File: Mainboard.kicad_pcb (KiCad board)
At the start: 4 copper layers, 90.2 x 95.9 mm, 244 parts, among them J1 USB_C_Receptacle_USB2.0, J10 200528-0100, J11 200528-0100, J12 200528-0100, J13 200528-0100, J14 200528-0100, J15 200528-0100, J16 200528-0100, J17 200528-0100, J18 200528-0100, J19 Conn_01x09, J2 282834-4, J20 Conn_01x04, J21 Conn_01x06, J22 U.FL-R-SMT-1, J23 U.FL-R-SMT-1, J24 Conn_02x05_Odd_Even, J3 282834-4, J4 1985807, J5 1985807, J6 1985807, J7 USB_C_Receptacle_USB2.0, J8 Micro_SD_Card_Det2, J9 Conn_02x05_Odd_Even, Q1 IRLML2803, Q10 MBT2222ADW1T1, Q11 BSS138DWQ-7, Q12 MBT2222ADW1T1, Q13 BSS138DWQ-7, Q14 MBT2222ADW1T1, Q15 BSS138DWQ-7, Q16 MMBT2907, Q17 MMBT2907, Q18 IRLML2803, Q19 IRF7404, Q2 MBT2222ADW1T1, Q21 IRLML2803, Q22 IRLML2803, Q23 IRF7404, Q3 MBT2222ADW1T1, Q4 MBT2222ADW1T1, Q5 BSS138DWQ-7, Q6 MBT2222ADW1T1, Q7 BSS138DWQ-7, Q8 MBT2222ADW1T1, Q9 BSS138DWQ-7, SW1 KMR231NG LFS, SW2 KMR231NG LFS, U1 MAX706RESA+, U10 ATSAMD21E18A-A, U11 MAX706RESA+, U12 E22-900M30S, U13 S1216V8, U14 EP2W+, U15 USBLC6-2SC6, U16 USBLC6-2SC6, U2 ATSAMD51J20A-AU, U3 BMX160, U4 DS3231S, U5 MR25H40MDF, U6 TPS7A4501DCQT, U7 TPS54226PWPR, U8 BQ25883RGER, U9 ADM1176-1ARMZ-R7, Y1 32.768kHz, Y2 32.768kHz

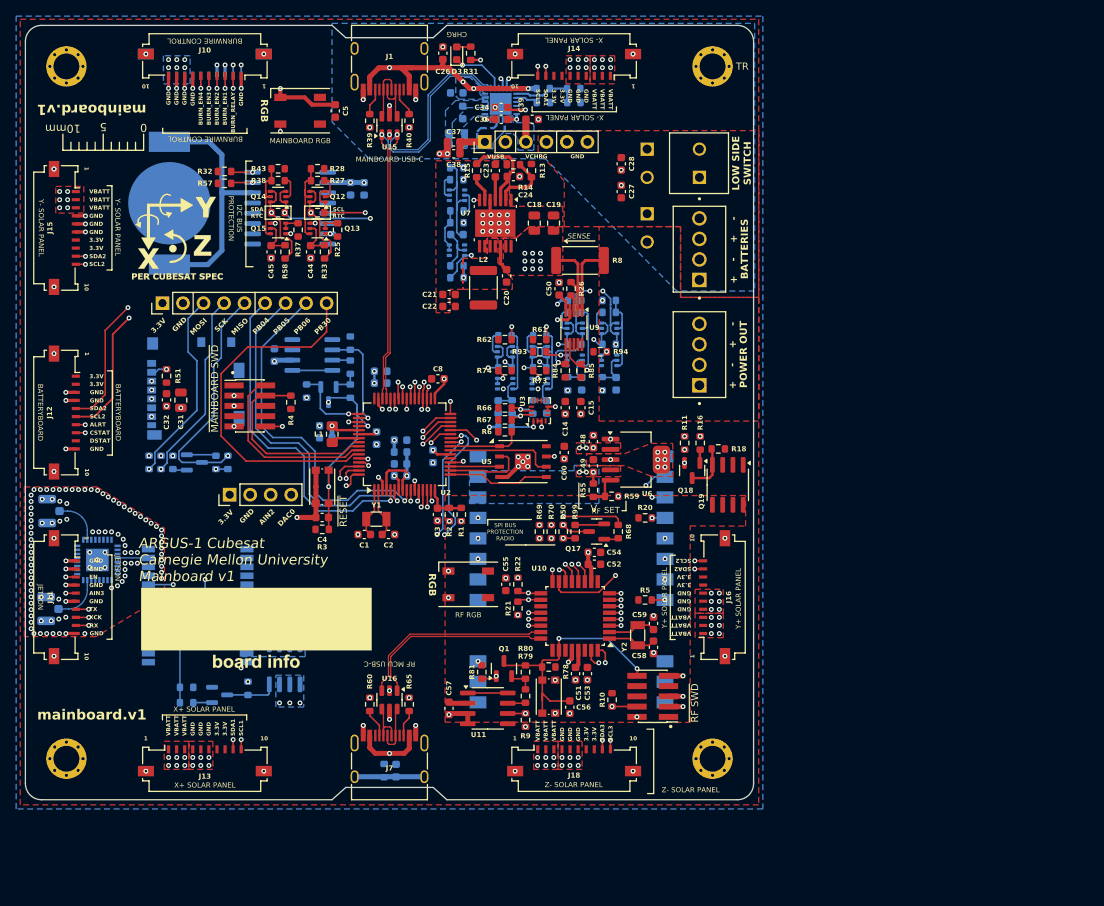
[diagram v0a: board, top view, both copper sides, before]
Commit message: Updated Mounting Holes
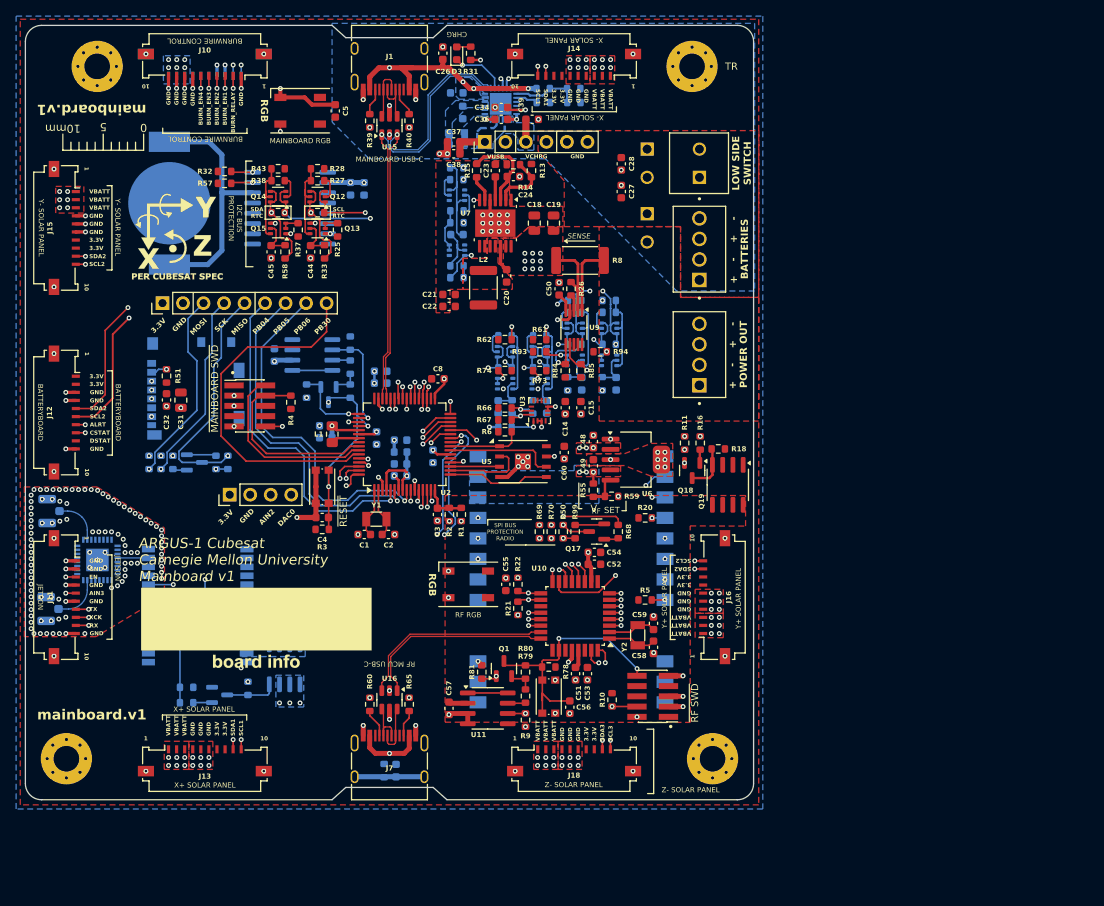
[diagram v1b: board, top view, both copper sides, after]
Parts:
- H1, H2, H3, H4: footprint mainboard:MountingHole -> mainboard:MountingHole2
- moved H1 3.81 mm to (108.6, 58.4)
- moved H2 2.54 mm to (182.2, 58.4)
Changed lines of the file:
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@@
 		)
 	)
-	(footprint "mainboard:MountingHole"
+	(footprint "mainboard:MountingHole2"
 		(layer "F.Cu")
-		(at 104.775 58.42)
+		(at 108.585 58.42)
 		(descr "Mounting Hole 3.2mm, M3")
 		(tags "mounting hole 3.2mm m3")
@@
 			)
 		)
-		(property "Footprint" "mainboard:MountingHole"
+		(property "Footprint" "mainboard:MountingHole2"
 			(at 0 0 0)
 			(layer "F.Fab")
@@
 		)
 		(pad "1" thru_hole circle
-			(at -2.05 0)
+			(at -2.38125 0 180)
 			(size 0.762 0.762)
 			(drill 0.381)
@@
 		)
 		(pad "1" thru_hole circle
-			(at -1.4495 -1.4495)
+			(at -1.683798 -1.683798 315)
 			(size 0.762 0.762)
 			(drill 0.381)
@@
 		)
 		(pad "1" thru_hole circle
-			(at -1.4495 1.4495)
+			(at -1.683798 1.683798 315)
 			(size 0.762 0.762)
 			(drill 0.381)
@@
 		)
 		(pad "1" thru_hole circle
-			(at 0 -2.05)
+			(at 0 -2.38125 180)
 			(size 0.762 0.762)
 			(drill 0.381)
@@
 		(pad "1" thru_hole circle
 			(at 0 0)
-			(size 5 5)
-			(drill 3.2)
+			(size 6.35 6.35)
+			(drill 3.175)
 			(layers "*.Cu" "*.Mask")
 			(remove_unused_layers no)
@@
 		)
 		(pad "1" thru_hole circle
-			(at 0 2.05)
+			(at 0 2.38125 180)
 			(size 0.762 0.762)
 			(drill 0.381)
@@
 		)
 		(pad "1" thru_hole circle
-			(at 1.4495 -1.4495)
+			(at 1.683798 -1.683798 315)
 			(size 0.762 0.762)
 			(drill 0.381)
@@
 		)
 		(pad "1" thru_hole circle
-			(at 1.4495 1.4495)
+			(at 1.683798 1.683798 315)
 			(size 0.762 0.762)
 			(drill 0.381)
@@
 		)
 		(pad "1" thru_hole circle
-			(at 2.05 0)
+			(at 2.38125 0 180)
 			(size 0.762 0.762)
 			(drill 0.381)
@@
 		)
 	)
-	(footprint "mainboard:MountingHole"
+	(footprint "mainboard:MountingHole2"
 		(layer "F.Cu")
 		(at 184.785 144.145)
@@
 			)
 		)
-		(property "Footprint" "mainboard:MountingHole"
+		(property "Footprint" "mainboard:MountingHole2"
 			(at 0 0 0)
 			(layer "F.Fab")
@@
 		)
 		(pad "1" thru_hole circle
-			(at -2.05 0)
+			(at -2.38125 0 180)
 			(size 0.762 0.762)
 			(drill 0.381)
@@
 		)
 		(pad "1" thru_hole circle
-			(at -1.4495 -1.4495)
+			(at -1.683798 -1.683798 315)
 			(size 0.762 0.762)
 			(drill 0.381)
@@
 		)
 		(pad "1" thru_hole circle
-			(at -1.4495 1.4495)
+			(at -1.683798 1.683798 315)
 			(size 0.762 0.762)
 			(drill 0.381)
@@
 		)
 		(pad "1" thru_hole circle
-			(at 0 -2.05)
+			(at 0 -2.38125 180)
 			(size 0.762 0.762)
 			(drill 0.381)
@@
 		(pad "1" thru_hole circle
 			(at 0 0)
-			(size 5 5)
-			(drill 3.2)
+			(size 6.35 6.35)
+			(drill 3.175)
 			(layers "*.Cu" "*.Mask")
 			(remove_unused_layers no)
@@
 		)
 		(pad "1" thru_hole circle
-			(at 0 2.05)
+			(at 0 2.38125 180)
 			(size 0.762 0.762)
 			(drill 0.381)
@@
 		)
 		(pad "1" thru_hole circle
-			(at 1.4495 -1.4495)
+			(at 1.683798 -1.683798 315)
 			(size 0.762 0.762)
 			(drill 0.381)
@@
 		)
 		(pad "1" thru_hole circle
-			(at 1.4495 1.4495)
+			(at 1.683798 1.683798 315)
 			(size 0.762 0.762)
 			(drill 0.381)
@@
 		)
 		(pad "1" thru_hole circle
-			(at 2.05 0)
+			(at 2.38125 0 180)
 			(size 0.762 0.762)
 			(drill 0.381)
@@
 			(layers "F.Cu" "F.Paste" "F.Mask")
 			(net 4 "~{RESET}")
-			(pinfunction "P")
+			(pinfunction "P1")
 			(pintype "passive")
 		)
@@
 			(layers "F.Cu" "F.Paste" "F.Mask")
 			(net 4 "~{RESET}")
-			(pinfunction "P")
+			(pinfunction "P1")
 			(pintype "passive")
 		)
@@
 			(layers "F.Cu" "F.Paste" "F.Mask")
 			(net 6 "GND")
-			(pinfunction "S1")
+			(pinfunction "S")
 			(pintype "passive")
 		)
@@
 			(layers "F.Cu" "F.Paste" "F.Mask")
 			(net 6 "GND")
-			(pinfunction "S1")
+			(pinfunction "S")
 			(pintype "passive")
 		)
@@
 		)
 	)
-	(footprint "mainboard:MountingHole"
+	(footprint "mainboard:MountingHole2"
 		(layer "F.Cu")
-		(at 184.785 58.42)
+		(at 182.245 58.42)
 		(descr "Mounting Hole 3.2mm, M3")
 		(tags "mounting hole 3.2mm m3")
@@
 			)
 		)
-		(property "Footprint" "mainboard:MountingHole"
+		(property "Footprint" "mainboard:MountingHole2"
 			(at 0 0 0)
 			(layer "F.Fab")
@@
 		)
 		(pad "1" thru_hole circle
-			(at -2.05 0)
+			(at -2.38125 0 180)
 			(size 0.762 0.762)
 			(drill 0.381)
@@
 		)
 		(pad "1" thru_hole circle
-			(at -1.4495 -1.4495)
+			(at -1.683798 -1.683798 315)
 			(size 0.762 0.762)
 			(drill 0.381)
@@
 		)
 		(pad "1" thru_hole circle
-			(at -1.4495 1.4495)
+			(at -1.683798 1.683798 315)
 			(size 0.762 0.762)
 			(drill 0.381)
@@
 		)
 		(pad "1" thru_hole circle
-			(at 0 -2.05)
+			(at 0 -2.38125 180)
 			(size 0.762 0.762)
 			(drill 0.381)
@@
 		(pad "1" thru_hole circle
 			(at 0 0)
-			(size 5 5)
-			(drill 3.2)
+			(size 6.35 6.35)
+			(drill 3.175)
 			(layers "*.Cu" "*.Mask")
 			(remove_unused_layers no)
@@
 		)
 		(pad "1" thru_hole circle
-			(at 0 2.05)
+			(at 0 2.38125 180)
 			(size 0.762 0.762)
 			(drill 0.381)
@@
 		)
 		(pad "1" thru_hole circle
-			(at 1.4495 -1.4495)
+			(at 1.683798 -1.683798 315)
 			(size 0.762 0.762)
 			(drill 0.381)
@@
 		)
 		(pad "1" thru_hole circle
-			(at 1.4495 1.4495)
+			(at 1.683798 1.683798 315)
 			(size 0.762 0.762)
 			(drill 0.381)
@@
 		)
 		(pad "1" thru_hole circle
-			(at 2.05 0)
+			(at 2.38125 0 180)
 			(size 0.762 0.762)
 			(drill 0.381)
@@
 		)
 	)
-	(footprint "mainboard:MountingHole"
+	(footprint "mainboard:MountingHole2"
 		(layer "F.Cu")
 		(at 104.775 144.145)
@@
 			)
 		)
-		(property "Footprint" "mainboard:MountingHole"
+		(property "Footprint" "mainboard:MountingHole2"
 			(at 0 0 0)
 			(layer "F.Fab")
@@
 		)
 		(pad "1" thru_hole circle
-			(at -2.05 0)
+			(at -2.38125 0 180)
 			(size 0.762 0.762)
 			(drill 0.381)
@@
 		)
 		(pad "1" thru_hole circle
-			(at -1.4495 -1.4495)
+			(at -1.683798 -1.683798 315)
 			(size 0.762 0.762)
 			(drill 0.381)
@@
 		)
 		(pad "1" thru_hole circle
-			(at -1.4495 1.4495)
+			(at -1.683798 1.683798 315)
 			(size 0.762 0.762)
 			(drill 0.381)
@@
 		)
 		(pad "1" thru_hole circle
-			(at 0 -2.05)
+			(at 0 -2.38125 180)
 			(size 0.762 0.762)
 			(drill 0.381)
@@
 		(pad "1" thru_hole circle
 			(at 0 0)
-			(size 5 5)
-			(drill 3.2)
+			(size 6.35 6.35)
+			(drill 3.175)
 			(layers "*.Cu" "*.Mask")
 			(remove_unused_layers no)
@@
 		)
 		(pad "1" thru_hole circle
-			(at 0 2.05)
+			(at 0 2.38125 180)
 			(size 0.762 0.762)
 			(drill 0.381)
@@
 		)
 		(pad "1" thru_hole circle
-			(at 1.4495 -1.4495)
+			(at 1.683798 -1.683798 315)
 			(size 0.762 0.762)
 			(drill 0.381)
@@
 		)
 		(pad "1" thru_hole circle
-			(at 1.4495 1.4495)
+			(at 1.683798 1.683798 315)
 			(size 0.762 0.762)
 			(drill 0.381)
@@
 		)
 		(pad "1" thru_hole circle
-			(at 2.05 0)
+			(at 2.38125 0 180)
 			(size 0.762 0.762)
 			(drill 0.381)
@@
 	)
 	(gr_text "TR"
-		(at 188.468 58.42 0)
+		(at 187.1218 58.42 0)
 		(layer "F.SilkS")
 		(effects

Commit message: v1 Final
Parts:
- R59: value 2.5K -> 3.16K
- REF** (x2): moved to B.Cu
- moved REF** 56.6 mm to (117.9, 78.6), turned to 180 degrees
- moved REF** 56.0 mm to (107.8, 134.8), turned to 180 degrees
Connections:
- net JETSON_RX renamed JETSON_MISO
- net JETSON_TX renamed JETSON_MOSI
- net JETSON_XCK renamed JETSON_SCK
- J11 pad 1: GND -> 3.3V
- J11 pad 2: GND -> SDA1
- J11 pad 3: JETSON_EN -> SCL1
- J11 pad 4: GND -> JETSON_EN
- J11 pad 5: AIN3 -> GND
- J11 pad 6: GND -> JETSON_CS
- J19 pad 8: PB06 -> GND
- U2 pad 10: JETSON_EN -> JETSON_CS
- U2 pad 9: PB06 -> JETSON_EN
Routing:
- net AIN3: track 62.6 -> 0.00 mm, vias 2 -> 0
- net JETSON_CS: track 0.00 -> 61.9 mm, vias 0 -> 2
- net PB06: track 44.5 -> 0.00 mm, vias 1 -> 0
- net SCL1: track 145.8 -> 185.9 mm, vias 6 -> 9
- net SDA1: track 136.8 -> 176.1 mm, vias 6 -> 9
- net 3.3V: track 14.8 -> 31.3 mm, vias 18 -> 20
- net GND: track 79.0 -> 75.3 mm, vias 246 -> 240
- net JETSON_EN: track 61.9 -> 61.3 mm
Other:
- board text removed: "AIN3"
- board text removed: "RX"
- board text removed: "TX"
- board text removed: "XCK"

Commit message: v1.1 Schematic
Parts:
- added C61: 0.1uF, Capacitor_SMD:C_0603_1608Metric, F.Cu at (168.4, 120.4)
- added C62: 0.1uF, Capacitor_SMD:C_0603_1608Metric, F.Cu at (164.8, 133.1)
- added C63: 0.1uF, Capacitor_SMD:C_0603_1608Metric, F.Cu at (204.9, 129.1)
- added C64: 0.1uF, Capacitor_SMD:C_0603_1608Metric, F.Cu at (166.1, 120.4)
- added C65: 0.1uF, Capacitor_SMD:C_0603_1608Metric, F.Cu at (168.4, 133.1)
- added C66: 0.1uF, Capacitor_SMD:C_0603_1608Metric, F.Cu at (173.8, 126.3)
- added C67: 10uF, Capacitor_SMD:C_0603_1608Metric, F.Cu at (160.2, 120.4)
- added C68: 10uF, Capacitor_SMD:C_0603_1608Metric, F.Cu at (163.1, 120.4)
- added C69: 0.1uF, Capacitor_SMD:C_0603_1608Metric, F.Cu at (164.6, 120.4)
- added C70: 0.1uF, Capacitor_SMD:C_0603_1608Metric, F.Cu at (161.0, 126.7)
- added C71: 1uF, Capacitor_SMD:C_0603_1608Metric, F.Cu at (208.9, 124.1)
- added D4: GREEN LED, LED_SMD:LED_0603_1608Metric, F.Cu at (222.6, 128.1)
- added FB2: FerriteBead_Small, Inductor_SMD:L_0603_1608Metric, F.Cu at (161.7, 120.4)
- added R100: 27R, Resistor_SMD:R_0603_1608Metric, F.Cu at (157.1, 126.4)
- added R101: 27R, Resistor_SMD:R_0603_1608Metric, F.Cu at (157.1, 124.9)
- added R102: 0R, Resistor_SMD:R_0603_1608Metric, F.Cu at (212.9, 121.6)
- added R103: 0R, Resistor_SMD:R_0603_1608Metric, F.Cu at (212.9, 124.1)
- added R104: 10K, Resistor_SMD:R_0603_1608Metric, F.Cu at (212.9, 126.6)
- added R105: 1K, Resistor_SMD:R_0603_1608Metric, F.Cu at (227.5, 130.4)
- added SW3: KMR231NG LFS, Button_Switch_SMD:SW_Push_1P1T_NO_CK_KMR2, F.Cu at (228.8, 126.9)
- added U17: RP2040, Package_DFN_QFN:QFN-56-1EP_7x7mm_P0.4mm_EP3.2x3.2mm, F.Cu at (167.4, 126.9)
- C54: value 10uF -> 0.1uF
- C58, C59: value 8pF -> 15pF
- R10: value 10K -> 1K
- U10: value ATSAMD21E18A-A -> MR25H40MDF; footprint Package_QFP:TQFP-32_7x7mm_P0.8mm -> Package_DFN_QFN:DFN-8-1EP_6x5mm_P1.27mm_EP2x2mm
- Y2: value 32.768kHz -> ABM8-272-T3; footprint Crystal:Crystal_SMD_3215-2Pin_3.2x1.5mm -> Crystal:Crystal_SMD_3225-4Pin_3.2x2.5mm
- moved D2 66.0 mm to (212.5, 91.0), turned to -90 degrees
- moved C55 64.3 mm to (212.5, 86.6), turned to 180 degrees
- moved C57 60.6 mm to (205.8, 109.8), turned to 0 degrees
- moved R9 60.1 mm to (207.3, 100.3), turned to 0 degrees
- moved U11 58.9 mm to (205.8, 105.0), turned to 90 degrees
- moved R79 55.9 mm to (204.3, 100.3), turned to 0 degrees
- moved J24 54.3 mm to (222.1, 105.6)
- moved R81 52.9 mm to (201.3, 105.7), turned to 180 degrees
- moved R80 51.7 mm to (201.3, 100.3), turned to 0 degrees
- moved Q1 51.6 mm to (200.9, 103.0), turned to 180 degrees
- moved R22 49.6 mm to (208.9, 134.1), turned to 0 degrees
- moved R21 48.6 mm to (208.9, 131.6), turned to 0 degrees
- moved C56 44.3 mm to (205.9, 116.3), turned to -90 degrees
- moved SW2 42.8 mm to (202.3, 116.3), turned to 180 degrees
- moved R78 37.9 mm to (198.6, 116.3), turned to -90 degrees
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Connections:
- C51 pad 1: Net-(U10-VDDCORE) -> +1V2
- C52 pad 1: RF_3.3V -> +1V2
- C53 pad 1: RF_3.3V -> +1V2
- C56 pad 2: ~{SAMD21_RST} -> ~{RF_RST}
- C58 pad 1: Net-(U10-PA00) -> Net-(U17-XIN)
- C59 pad 1: Net-(U10-PA01) -> Net-(C59-Pad1)
- D2 pad 4: /RF and GPS/SAMD21_NEOPIXEL -> /RF and GPS/RF_NEOPIXEL
- J24 pad 10: ~{SAMD21_RST} -> ~{RF_RST}
- J24 pad 2: SAMD21_SWD -> RF_SWD
- J24 pad 4: SAMD21_SWC -> RF_SWC
- Q1 pad 1: SAMD21_WDT_EN -> RF_WDT_EN
- Q1 pad 3: ~{SAMD21_RST} -> ~{RF_RST}
- R10 pad 1: RF_3.3V -> Net-(U17-XOUT)
- R10 pad 2: SAMD21_SWC -> Net-(C59-Pad1)
- R78 pad 2: ~{SAMD21_RST} -> ~{RF_RST}
- R80 pad 1: ~{SAMD21_RST} -> ~{RF_RST}
- R81 pad 1: SAMD21_WDT_EN -> RF_WDT_EN
- R9 pad 1: SAMD21_WDT_WDI -> RF_WDT_WDI
- SW2 pad 1: ~{SAMD21_RST} -> ~{RF_RST}
- U10 pad 1: Net-(U10-PA00) -> /RF and GPS/QSPI_SS
- U10 pad 2: Net-(U10-PA01) -> /RF and GPS/QSPI_D1
- U10 pad 3: RF_RST -> /RF and GPS/QSPI_D2
- U10 pad 4: RF_BUSY -> GND
- U10 pad 5: RF_CS -> /RF and GPS/QSPI_D0
- U10 pad 6: RF_MISO -> /RF and GPS/QSPI_SCK
- U10 pad 7: RF_MOSI -> /RF and GPS/QSPI_D3
- U10 pad 8: RF_SCK -> RF_3.3V
- U10 pad 9: RF_3.3V -> GND
- U11 pad 6: SAMD21_WDT_WDI -> RF_WDT_WDI
- Y2 pad 1: Net-(U10-PA00) -> Net-(U17-XIN)
- Y2 pad 2: Net-(U10-PA01) -> GND
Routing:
- net ~{SAMD21_RST}: track 32.4 -> 0.00 mm, vias 2 -> 0
- net ~{RF_RST}: track 0.00 -> 18.5 mm
- net GND: track 75.3 -> 60.4 mm, vias 240 -> 224
- net /RF and GPS/QSPI_SS: track 0.00 -> 14.8 mm
- net SAMD21_WDT_WDI: track 14.7 -> 0.00 mm, vias 2 -> 0
- net /RF and GPS/QSPI_D1: track 0.00 -> 13.3 mm
- net USB_D2-: track 24.7 -> 11.8 mm
- net USB_D2+: track 24.3 -> 11.4 mm
- net +1V2: track 0.00 -> 12.4 mm
- net /RF and GPS/SAMD21_NEOPIXEL: track 12.2 -> 0.00 mm, vias 2 -> 0
- net SAMD21_WDT_EN: track 12.0 -> 0.00 mm, vias 2 -> 0
- net /RF and GPS/QSPI_D2: track 0.00 -> 11.8 mm
- net SAMD21_SWD: track 11.7 -> 0.00 mm, vias 2 -> 0
- net SAMD21_SWC: track 11.4 -> 0.00 mm, vias 2 -> 0
- net RF_WDT_WDI: track 0.00 -> 11.0 mm
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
